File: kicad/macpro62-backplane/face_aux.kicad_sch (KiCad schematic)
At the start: 0 parts

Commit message: Cross-board compatibility audit: interface control doc, CR-BP-1 applied, J2/J3 row-swap pinouts, 15-pin face AUX, fan header removed from backplane, CPU board i226/BT1 cleanup
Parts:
- added #BLK3: STUB_FACE_AUX, symbol MP62:STUB_FACE_AUX
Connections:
- net 3V3_BP: now also #BLK3.13 (3V3_BP)
- net 3V3_SB: now also #BLK3.12 (3V3_SB)
- net FACE_PRSNT_N: now also #BLK3.3 (FACE_PRSNT_N)
- net FACE_PWR_EN: now also #BLK3.1 (FACE_PWR_EN)
- net FACE_PWR_GOOD: now also #BLK3.2 (FACE_PWR_GOOD)
- net FACE_SMB_ALERT_N: now also #BLK3.6 (FACE_SMB_ALERT_N)
- net FACE_SMB_SCL: now also #BLK3.4 (FACE_SMB_SCL)
- net FACE_SMB_SDA: now also #BLK3.5 (FACE_SMB_SDA)
- net FACE_THERM_ALERT_N: now also #BLK3.7 (FACE_THERM_ALERT_N)
- net FACE_THERM_TRIP_N: now also #BLK3.8 (FACE_THERM_TRIP_N)
- net FACE_USB_DN: now also #BLK3.10 (FACE_USB_DN)
- net FACE_USB_DP: now also #BLK3.9 (FACE_USB_DP)
- new net FACE_MOD_LED_N: #BLK3.11 (FACE_MOD_LED_N)
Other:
- note added: "- FACE_PWR_EN / FACE_PWR_GOOD, PRSNT#, SMBus (ID EEPROM 0x50, TMP1075 0x48, extra 0x49-0x4F), THERM_ALERT#, THERM_TRIP#, USB2 (primary), MOD_LED# (pin 15), 3V3_AUX"
- note added: "- J3 (Face P) / J4 (Face S): JST GH 15P (BM15B vertical) AUX cable BP -> face J_AUX; pinout = MP62-FACE v0.1 aux_gh15.csv (1:1)"
- note removed: "- FACE_PWR_EN / FACE_PWR_GOOD, PRSNT#, SMBus (ID EEPROM 0x50, LM75 0x48), THERM_ALERT#, THERM_TRIP#, USB2, 3V3_AUX"
- note removed: "- J3 (Face P) / J4 (Face S): JST GH 14P low-speed AUX cable BP -> face module"
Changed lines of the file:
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@@
 	(title_block
 		(title "MP62 backplane: Face AUX link (instanced for Face P and Face S)")
-		(date "2026-10-01")
-		(rev "A-bd1")
-		(comment 1 "Block stub: hierarchical labels only, circuit TBD")
+		(date "2026-10-02")
+		(rev "A-bd2")
+		(comment 1 "Block stub: hierarchical labels + one non-BOM stub symbol (#BLKn, passive pins) so ERC sees the nets; circuit TBD")
 	)
 	(hierarchical_label "FACE_PWR_EN"
@@
 		(effects (font (size 1.27 1.27)) (justify right))
 	)
+	(hierarchical_label "FACE_MOD_LED_N"
+		(shape output)
+		(at 38.1 55.88 180)
+		(effects (font (size 1.27 1.27)) (justify right))
+	)
 	(hierarchical_label "3V3_SB"
 		(shape input)
-		(at 38.1 55.88 180)
+		(at 38.1 58.42 180)
 		(effects (font (size 1.27 1.27)) (justify right))
 	)
 	(hierarchical_label "3V3_BP"
 		(shape input)
-		(at 38.1 58.42 180)
+		(at 38.1 60.96 180)
 		(effects (font (size 1.27 1.27)) (justify right))
+	)
+	(symbol
+		(lib_id "MP62:STUB_FACE_AUX")
+		(at 38.1 30.48 0)
+		(unit 1)
+		(exclude_from_sim yes)
+		(in_bom no)
+		(on_board no)
+		(dnp no)
+		(property "Reference" "#BLK3"
+			(at 40.64 27.94 0)
+			(effects (font (size 1.27 1.27)) (justify left) (hide yes))
+		)
+		(property "Value" "STUB_FACE_AUX"
+			(at 40.64 26.67 0)
+			(effects (font (size 1.27 1.27)) (justify left) (hide yes))
+		)
+		(pin "1"
+		)
+		(pin "2"
+		)
+		(pin "3"
+		)
+		(pin "4"
+		)
+		(pin "5"
+		)
+		(pin "6"
+		)
+		(pin "7"
+		)
+		(pin "8"
+		)
+		(pin "9"
+		)
+		(pin "10"
+		)
+		(pin "11"
+		)
+		(pin "12"
+		)
+		(pin "13"
+		)
+		(instances
+			(project "backplane"
+				(path "/6a1c2d3e-0000-4000-8000-000000000062/515a069b-42b9-4028-9586-20f17569eacf"
+					(reference "#BLK3")
+					(unit 1)
+				)
+				(path "/6a1c2d3e-0000-4000-8000-000000000062/934efb3c-edbd-4eaa-b03f-aad22b5c7996"
+					(reference "#BLK4")
+					(unit 1)
+				)
+			)
+		)
 	)
 	(text "BLOCK STUB (rev A block diagram). Contents planned:"
@@
 		(effects (font (size 1.5 1.5)) (justify left bottom))
 	)
-	(text "- J3 (Face P) / J4 (Face S): JST GH 14P low-speed AUX cable BP -> face module"
+	(text "- J3 (Face P) / J4 (Face S): JST GH 15P (BM15B vertical) AUX cable BP -> face J_AUX; pinout = MP62-FACE v0.1 aux_gh15.csv (1:1)"
 		(exclude_from_sim no)
 		(at 76.20 35.56 0)
 		(effects (font (size 1.27 1.27)) (justify left bottom))
 	)
-	(text "- FACE_PWR_EN / FACE_PWR_GOOD, PRSNT#, SMBus (ID EEPROM 0x50, LM75 0x48), THERM_ALERT#, THERM_TRIP#, USB2, 3V3_AUX"
+	(text "- FACE_PWR_EN / FACE_PWR_GOOD, PRSNT#, SMBus (ID EEPROM 0x50, TMP1075 0x48, extra 0x49-0x4F), THERM_ALERT#, THERM_TRIP#, USB2 (primary), MOD_LED# (pin 15), 3V3_AUX"
 		(exclude_from_sim no)
 		(at 76.20 39.37 0)

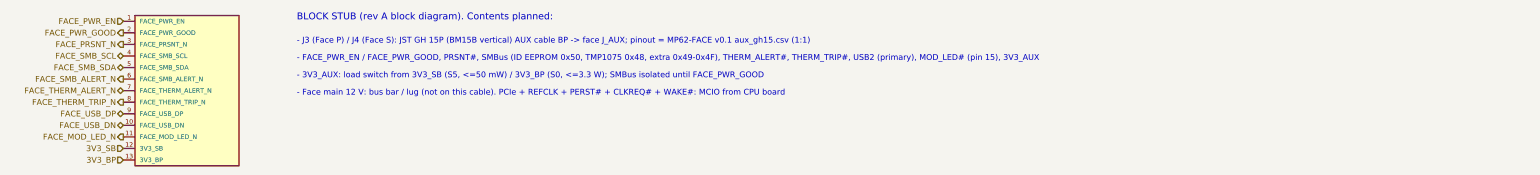
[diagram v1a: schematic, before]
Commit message: ICD rev 2: 45 deg faces, 445 W ceiling + live power target (INA228 telemetry), ribbon MCIO jog cables, BT on S0, fan fail-safe, port-module I2C map
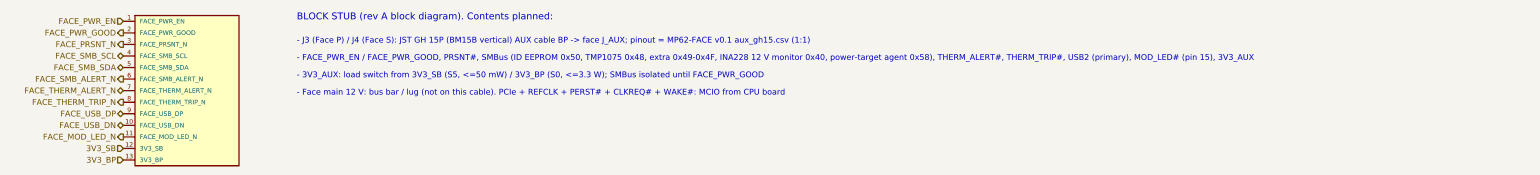
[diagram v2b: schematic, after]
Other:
- note added: "- FACE_PWR_EN / FACE_PWR_GOOD, PRSNT#, SMBus (ID EEPROM 0x50, TMP1075 0x48, extra 0x49-0x4F, INA228 12 V monitor 0x40, power-target agent 0x58), THERM_ALERT#, THERM_TRIP#, USB2 (primary), MOD_LED# (pin 15), 3V3_AUX"
- note removed: "- FACE_PWR_EN / FACE_PWR_GOOD, PRSNT#, SMBus (ID EEPROM 0x50, TMP1075 0x48, extra 0x49-0x4F), THERM_ALERT#, THERM_TRIP#, USB2 (primary), MOD_LED# (pin 15), 3V3_AUX"
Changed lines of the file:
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@@
 		(instances
 			(project "backplane"
-				(path "/6a1c2d3e-0000-4000-8000-000000000062/515a069b-42b9-4028-9586-20f17569eacf"
+				(path "/6a1c2d3e-0000-4000-8000-000000000062/90c3c672-f426-496a-b3c2-b6ca9489d7a2"
 					(reference "#BLK3")
 					(unit 1)
 				)
-				(path "/6a1c2d3e-0000-4000-8000-000000000062/934efb3c-edbd-4eaa-b03f-aad22b5c7996"
+				(path "/6a1c2d3e-0000-4000-8000-000000000062/a59d0054-6df6-490c-b4e3-8623e300e706"
 					(reference "#BLK4")
 					(unit 1)
@@
 		(effects (font (size 1.27 1.27)) (justify left bottom))
 	)
-	(text "- FACE_PWR_EN / FACE_PWR_GOOD, PRSNT#, SMBus (ID EEPROM 0x50, TMP1075 0x48, extra 0x49-0x4F), THERM_ALERT#, THERM_TRIP#, USB2 (primary), MOD_LED# (pin 15), 3V3_AUX"
+	(text "- FACE_PWR_EN / FACE_PWR_GOOD, PRSNT#, SMBus (ID EEPROM 0x50, TMP1075 0x48, extra 0x49-0x4F, INA228 12 V monitor 0x40, power-target agent 0x58), THERM_ALERT#, THERM_TRIP#, USB2 (primary), MOD_LED# (pin 15), 3V3_AUX"
 		(exclude_from_sim no)
 		(at 76.20 39.37 0)
